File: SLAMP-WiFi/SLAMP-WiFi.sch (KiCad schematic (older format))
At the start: 49 parts, among them P1 POWER_IN 5V, P10 FACE5, P2 USB_BUS, P3 VUSB, P4 EXTRA, P5 ADC, P6 FACE1, P7 FACE2, P8 FACE3, P9 FACE4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

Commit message: Serigrafia terminada
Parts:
- SW1, SW2: footprint (none) -> Buttons_Switches_THT:SW_PUSH_6mm
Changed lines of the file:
@@
 F 0 "SW2" H 10800 5400 50  0000 L CNN
 F 1 "KEY_FLASH" H 10750 5240 50  0000 C CNN
-F 2 "" H 10750 5500 50  0001 C CNN
+F 2 "Buttons_Switches_THT:SW_PUSH_6mm" H 10750 5500 50  0001 C CNN
 F 3 "" H 10750 5500 50  0001 C CNN
 	1    10750 5300
@@
 F 0 "SW1" H 9650 5800 50  0000 L CNN
 F 1 "KEY_RST" H 9600 5640 50  0000 C CNN
-F 2 "" H 9600 5900 50  0001 C CNN
+F 2 "Buttons_Switches_THT:SW_PUSH_6mm" H 9600 5900 50  0001 C CNN
 F 3 "" H 9600 5900 50  0001 C CNN
 	1    9600 5700

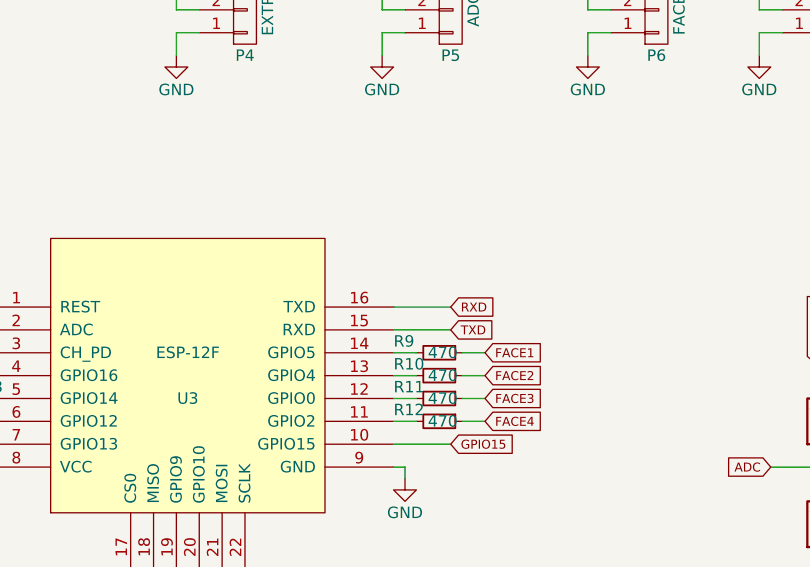
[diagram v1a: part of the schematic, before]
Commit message: Error con el GPIO0 arreglado
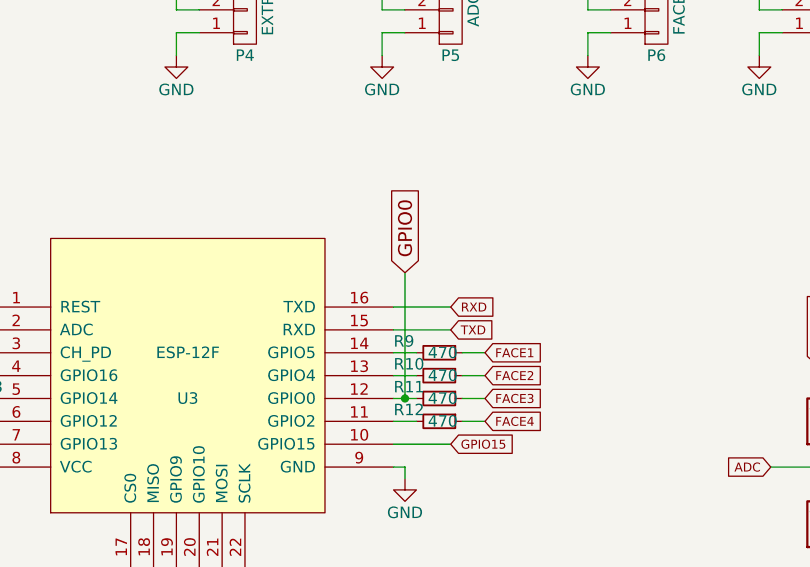
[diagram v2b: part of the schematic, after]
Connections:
- net GPIO0: now also R11.2, U3.12 (GPIO0)
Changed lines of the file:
@@
 	0    1    1    0
 $EndComp
+Wire Wire Line
+	6750 4900 6750 4350
+Connection ~ 6750 4900
+Text GLabel 6750 4350 1    60   Input ~ 0
+GPIO0
 $EndSCHEMATC

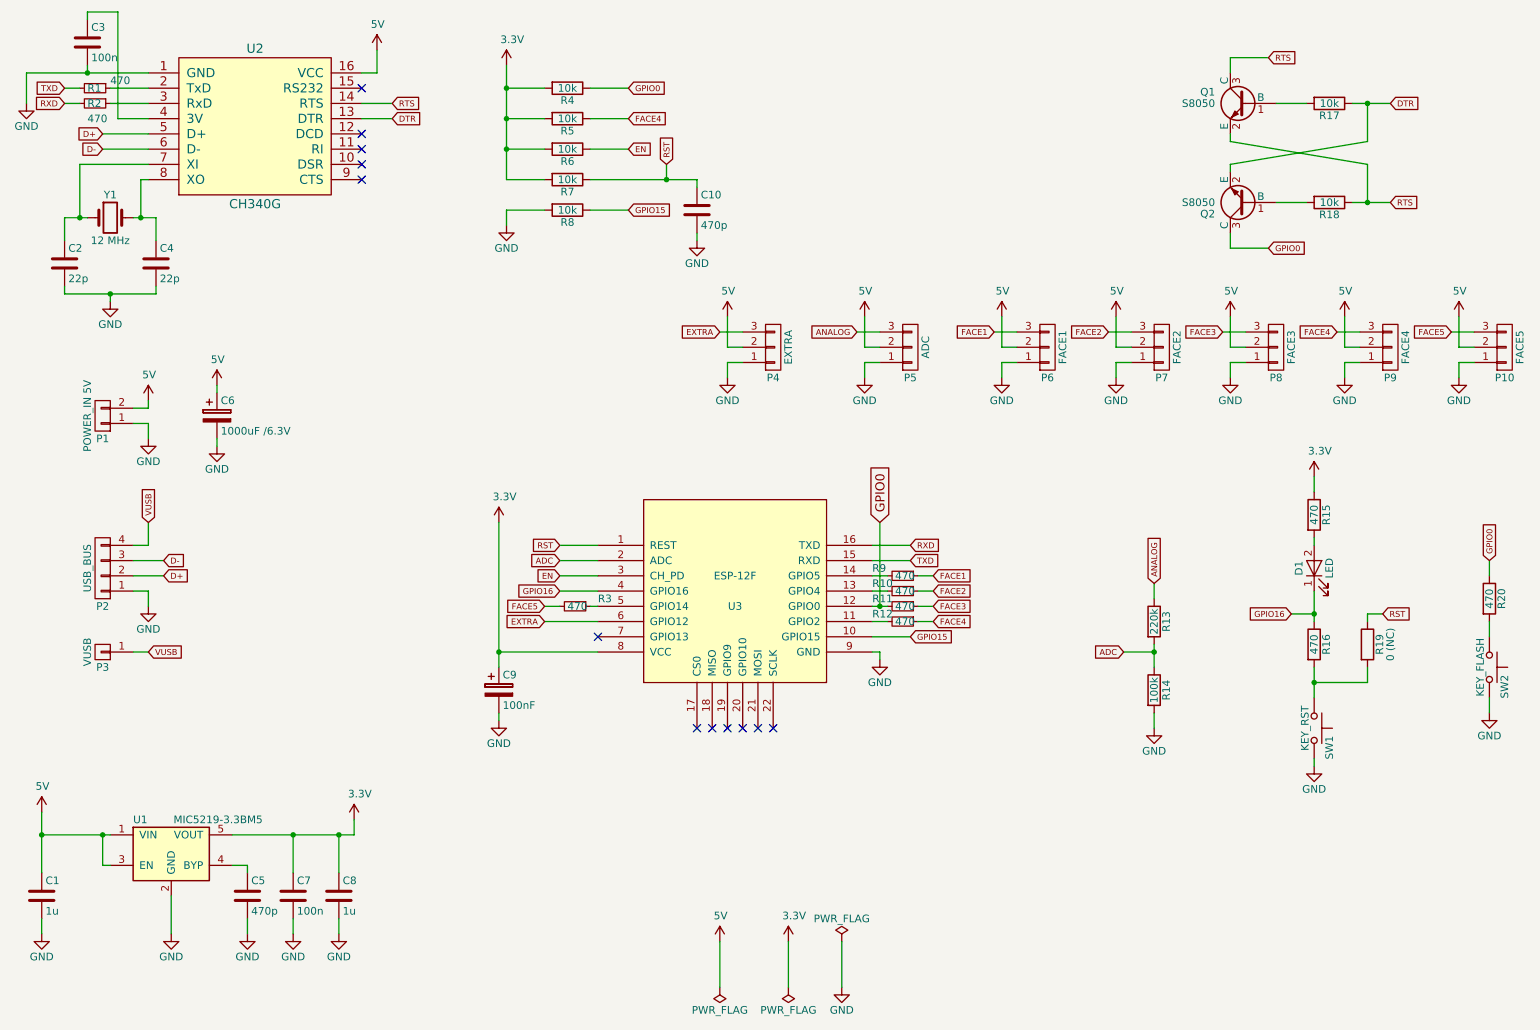
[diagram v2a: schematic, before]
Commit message: Problema con los RTS solucionado
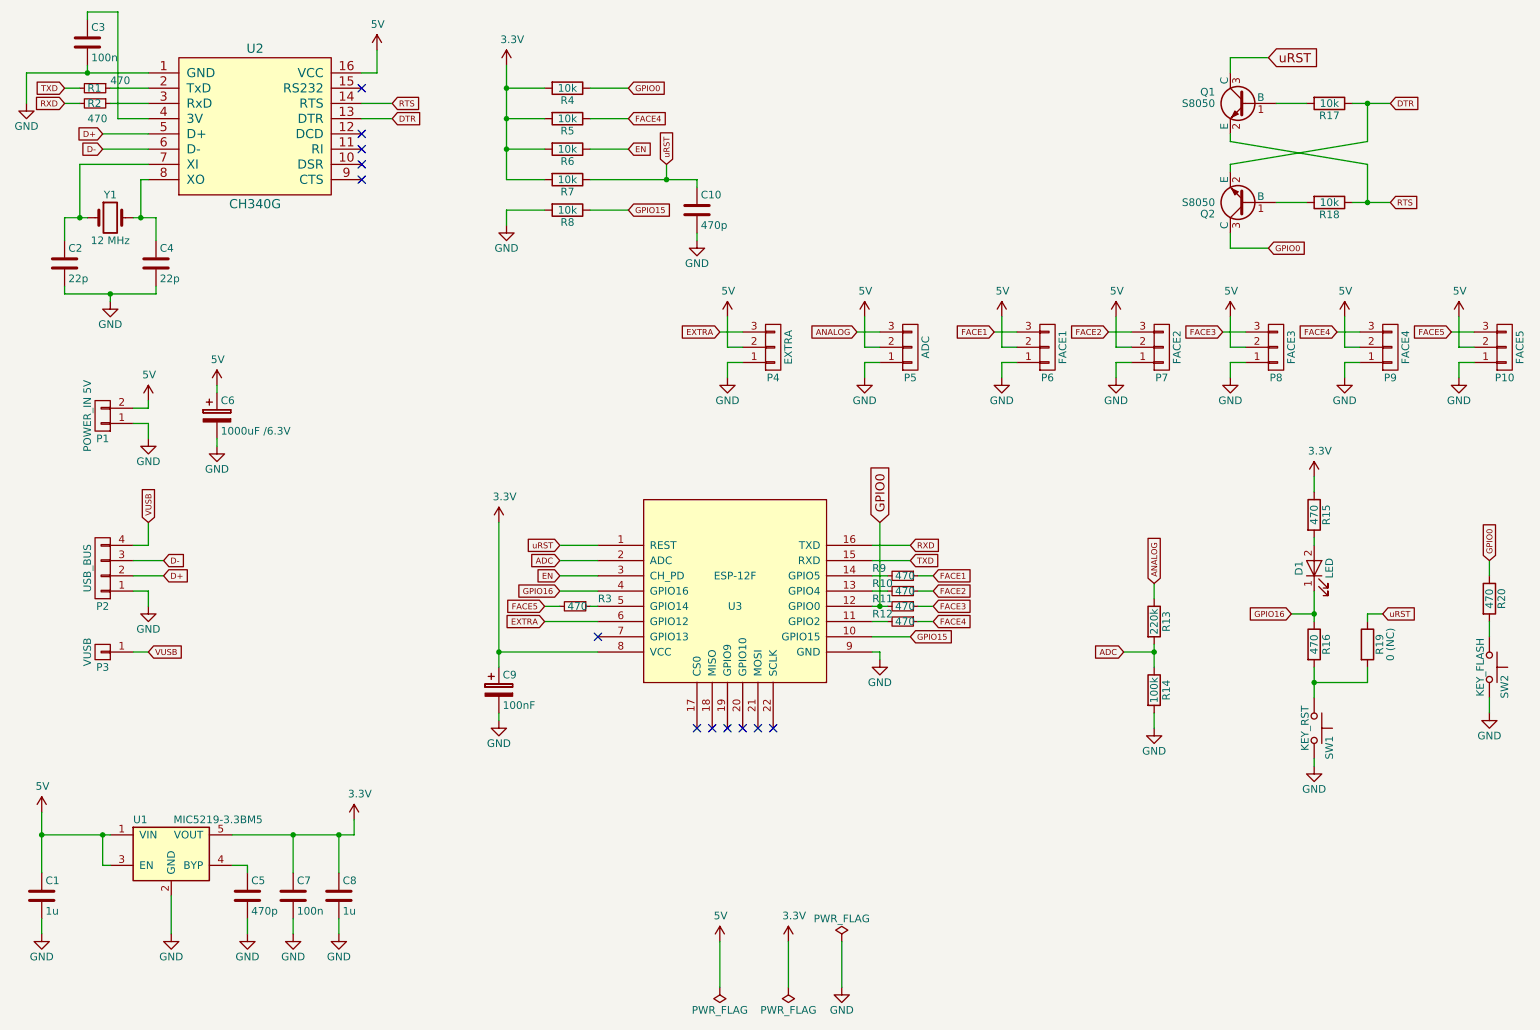
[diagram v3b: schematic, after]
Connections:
- net RTS: no longer Q1.3 (C)
- net RST renamed uRST
- net uRST: now also Q1.3 (C)
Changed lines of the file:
@@
 LIBS:contrib
 LIBS:valves
-LIBS:ESP32
-LIBS:74xgxx
-LIBS:5050_ws2811
-LIBS:a4988-module
-LIBS:ac-dc
-LIBS:acs712
-LIBS:actel
 LIBS:adafruit
-LIBS:adxl345
-LIBS:allegro
-LIBS:Altera
-LIBS:AMS1117
-LIBS:analog_devices
-LIBS:ant
-LIBS:at24c64
-LIBS:battery_management
-LIBS:bbd
-LIBS:bc56-12EWA
-LIBS:bosch
-LIBS:brooktre
-LIBS:cmos_ieee
-LIBS:cp2103
-LIBS:CP2102
-LIBS:dc-dc
-LIBS:dht11
-LIBS:diode
-LIBS:elec-unifil
-LIBS:er-oled-ssd1306
-LIBS:ESD_Protection
-LIBS:esp8266ex
-LIBS:esp8266-module
-LIBS:fe
-LIBS:frizzy_ICs
-LIBS:ft232rq
-LIBS:ftdi
-LIBS:Gajda_opto
 LIBS:GeekAmmo
-LIBS:gennum
-LIBS:graphic
-LIBS:GS6300
-LIBS:gy-a4988_module
-LIBS:hc11
-LIBS:hc541
-LIBS:hc-05
-LIBS:HC164
-LIBS:hlk-rm04
-LIBS:ir
-LIBS:irf7907
-LIBS:isp_6p
-LIBS:l298n
-LIBS:L9110
-LIBS:LargeKickstarter
-LIBS:Lattice
 LIBS:LilyPad-Wearables
-LIBS:LM2575
-LIBS:logo
-LIBS:logo-azura-wrench
-LIBS:lt1129cst
-LIBS:M25P05
-LIBS:max
-LIBS:max1538
-LIBS:maxim
-LIBS:mcp1640
-LIBS:mcp1640b
-LIBS:mcp73831
-LIBS:MCP3208
-LIBS:mechanical
-LIBS:microchip_dspic33dsc
-LIBS:microchip_pic10mcu
-LIBS:microchip_pic12mcu
-LIBS:microchip_pic16mcu
-LIBS:microchip_pic18mcu
-LIBS:microchip_pic32mcu
-LIBS:miniusb
-LIBS:motor_drivers
-LIBS:motors
-LIBS:mp2109dq
-LIBS:MP2307DN
-LIBS:mpu9250
-LIBS:msp430
-LIBS:na10-psu
-LIBS:nordicsemi
-LIBS:nrf24l01
-LIBS:nxp_armmcu
-LIBS:OF5032
-LIBS:onsemi
-LIBS:Oscillators
-LIBS:pl2303
-LIBS:pogopin
-LIBS:powerint
-LIBS:powerjack
-LIBS:Power_Management
-LIBS:pspice
-LIBS:pt4115
-LIBS:references
-LIBS:relays
-LIBS:rfcom
-LIBS:RJ45-ENCODER
-LIBS:rtl8196
-LIBS:rv3029c2
-LIBS:sensors
-LIBS:silabs
-LIBS:smd oscillator
-LIBS:songle_relay
 LIBS:SparkFun-Aesthetics
 LIBS:SparkFun-AnalogIC
@@
 LIBS:SparkFun-RF
 LIBS:SparkFun-Sensors
-LIBS:spiflash_16m
-LIBS:st1s10
-LIBS:stc12c5a60s2
-LIBS:stepper_drivers
-LIBS:stm8
-LIBS:stm32
-LIBS:STM32F100RBT6B
-LIBS:stpdn
-LIBS:supertex
-LIBS:switches
-LIBS:tcs3200d
-LIBS:tda5144
 LIBS:Teensy_3_and_LC_Series_Boards_v1.1
-LIBS:test
-LIBS:texas-msp
-LIBS:tlv70233
-LIBS:tp4056
-LIBS:transf
-LIBS:ts812c
-LIBS:ttl_ieee
-LIBS:usb_a
-LIBS:usb-a-pcb
-LIBS:usb_ax2
 LIBS:User-Submitted
-LIBS:video
-LIBS:w25q32bv
-LIBS:wiznet
-LIBS:Worldsemi
-LIBS:xc3s100etq144
-LIBS:xc3s500evq100
-LIBS:xc6slx9-tqg144
-LIBS:XC9572-TQ100
-LIBS:Xicor
-LIBS:xilinx_spartan3_virtex4_and_5
-LIBS:zetex
-LIBS:Zilog
-LIBS:рэс-49
-LIBS:тпг-1
-LIBS:ESP8266
-LIBS:CH340G_D-SUN-V3.0-cache
 LIBS:SLAMP-WiFi-cache
 EELAYER 25 0
@@
 RTS
 Wire Wire Line
-	9050 1400 9050 1300
-Wire Wire Line
-	9050 1300 9300 1300
-Wire Wire Line
 	9350 2250 9550 2250
 Wire Wire Line
@@
 Wire Wire Line
 	9050 2550 9300 2550
-Text GLabel 9300 1300 2    39   Input ~ 0
-RTS
 Text GLabel 9300 2550 2    39   Input ~ 0
 GPIO0
@@
 	4900 4800 4650 4800
 Text GLabel 4650 4500 0    39   Input ~ 0
-RST
+uRST
 Text GLabel 4650 4600 0    39   Input ~ 0
 ADC
@@
 EN
 Text GLabel 5350 2000 1    39   Input ~ 0
-RST
+uRST
 $Comp
 L GND #PWR07
@@
 	9950 4950 10050 4950
 Text GLabel 10050 4950 2    39   Input ~ 0
-RST
+uRST
 $Comp
 L GND #PWR018
@@
 Text GLabel 6750 4350 1    60   Input ~ 0
 GPIO0
+Wire Wire Line
+	9300 1300 9050 1300
+Wire Wire Line
+	9050 1300 9050 1400
+Text GLabel 9300 1300 2    60   Input ~ 0
+uRST
 $EndSCHEMATC

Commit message: Sensores tactiles añadidos
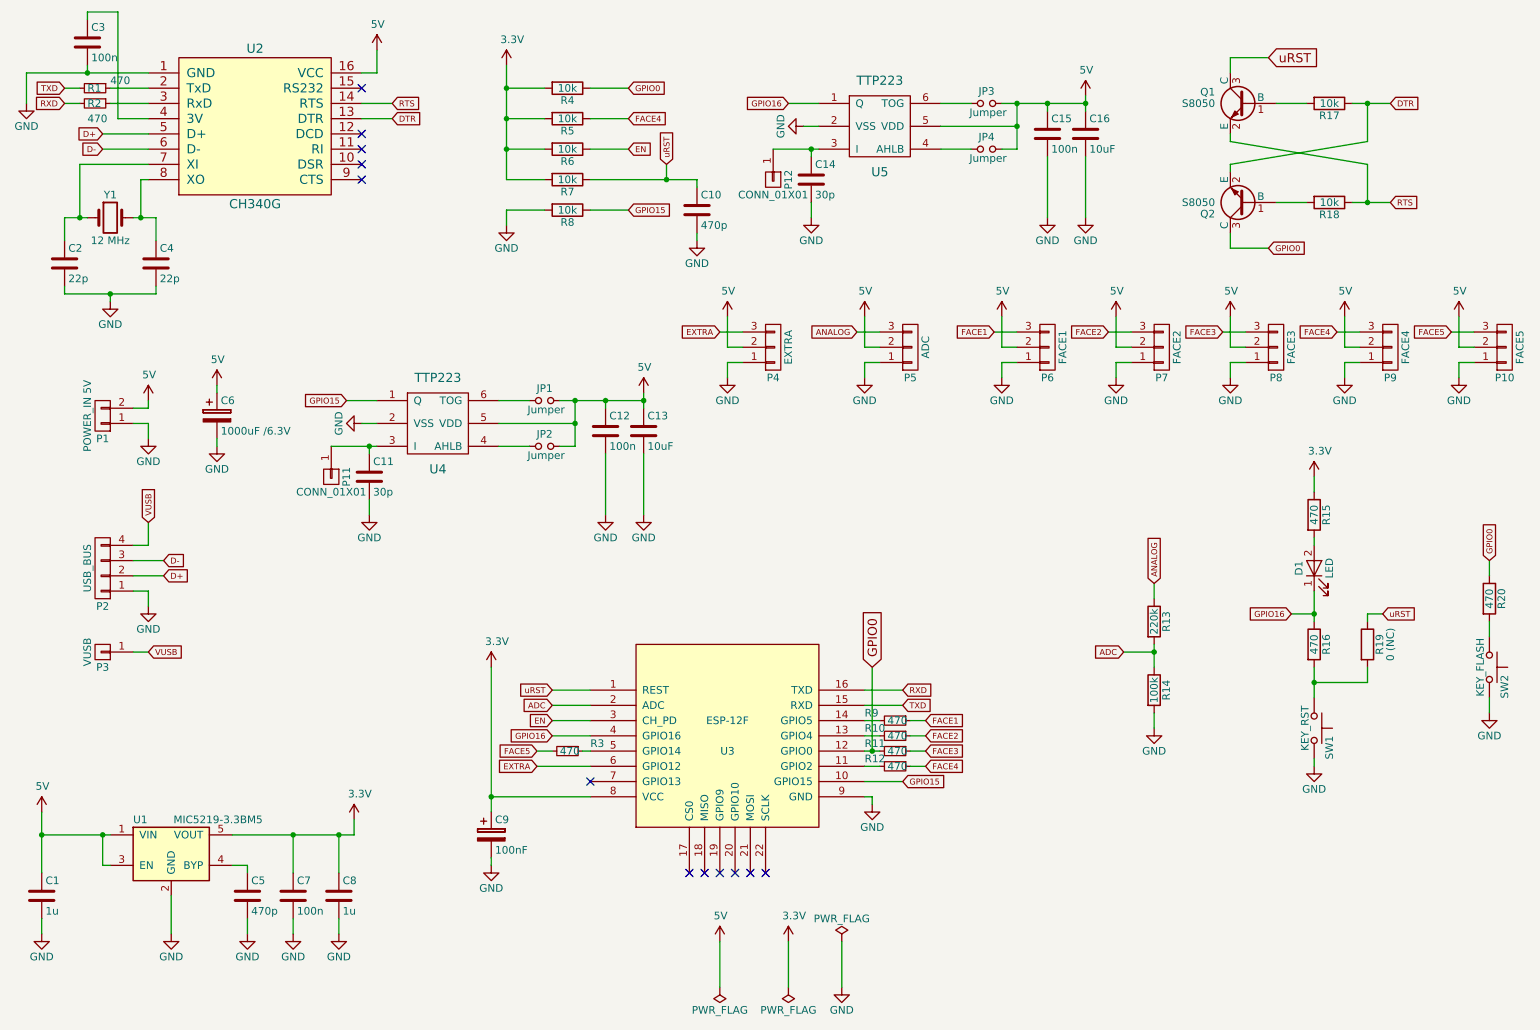
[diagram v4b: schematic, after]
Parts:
- added C11, C14: 30p, Capacitors_SMD:C_0805, symbol C
- added C12, C15: 100n, Capacitors_SMD:C_0805, symbol C
- added C13, C16: 10uF, Capacitors_SMD:C_0805, symbol C
- added JP1, JP2, JP3, JP4: Jumper, Resistors_SMD:R_0603, symbol Jumper_NO_Small
- added P11, P12: CONN_01X01, Connectors:1X01, symbol CONN_01X01
- added U4, U5: TTP223, TO_SOT_Packages_SMD:SOT-23-6, symbol TTP223
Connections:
- net 5V: now also C12.1, C13.1, C15.1, C16.1, JP1.2, JP2.2, JP3.2, JP4.2, U4.5 (VDD), U5.5 (VDD)
- net GND: now also C11.2, C12.2, C13.2, C14.2, C15.2, C16.2, U4.2 (VSS), U5.2 (VSS)
- net GPIO15: now also U4.1 (Q)
- net GPIO16: now also U5.1 (Q)
- new net: C11.1, P11.1 (P1), U4.3 (I)
- new net: JP2.1, U4.4 (AHLB)
- new net: JP1.1, U4.6 (TOG)
- new net: C14.1, P12.1 (P1), U5.3 (I)
- new net: JP4.1, U5.4 (AHLB)
- new net: JP3.1, U5.6 (TOG)
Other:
- moved on the sheet: C9, R10, R11, R12, R3, R9, U3
